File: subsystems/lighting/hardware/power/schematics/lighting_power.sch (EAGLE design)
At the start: 11 parts, among them J1 MOLEX-MICROLOCK-6PIN, J2 MOLEX-MICROLOCK-6PIN, J3 MOLEX-MICROLOCK-6PIN, J4 DCBARRELJACK

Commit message: Lighting V0.3
Fixed daisy-chaining "mirroring" problem
Made DC jack footprint holes smaller (3.3mm->3.1mm dia.)
Made Molex support pads NC
Minor routing updates
Updated silkscreen text
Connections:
- net GND: no longer J1.7, J1.8, J2.7, J2.8, J3.7, J3.8
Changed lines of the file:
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@@
 <part name="TP1" library="Test Point" library_urn="urn:adsk.wipprod:fs.file:vf.-YUoFGRWTEqdap1enj_r5g" deviceset="TP_CIRCLE_2.5MM" device="" package3d_urn="urn:adsk.wipprod:fs.file:vf.3FkuZaG9RiGo42nBWSli3w?version=2" value="GND"/>
 <part name="TP2" library="Test Point" library_urn="urn:adsk.wipprod:fs.file:vf.-YUoFGRWTEqdap1enj_r5g" deviceset="TP_CIRCLE_2.5MM" device="" package3d_urn="urn:adsk.wipprod:fs.file:vf.3FkuZaG9RiGo42nBWSli3w?version=2" value="VCC"/>
+<part name="J4" library="DC Barrel Jack (Locking)" library_urn="urn:adsk.wipprod:fs.file:vf.h4XB8JKWQlqKkOKCMBcezA" deviceset="DCBARRELJACK" device="" package3d_urn="urn:adsk.wipprod:fs.file:vf.mIvCFUCFT52mx3mRBPJ7Ng?version=3"/>
 <part name="J1" library="Molex Micro-Lock PLUS 6-Pin 90deg" library_urn="urn:adsk.wipprod:fs.file:vf.aLnYsiJBRyGIcsa2SAseLA" deviceset="MOLEX-MICROLOCK-6PIN" device="" package3d_urn="urn:adsk.wipprod:fs.file:vf.ZhRZvNezSJa09WGYEOUI9w?version=2"/>
 <part name="J2" library="Molex Micro-Lock PLUS 6-Pin 90deg" library_urn="urn:adsk.wipprod:fs.file:vf.aLnYsiJBRyGIcsa2SAseLA" deviceset="MOLEX-MICROLOCK-6PIN" device="" package3d_urn="urn:adsk.wipprod:fs.file:vf.ZhRZvNezSJa09WGYEOUI9w?version=2"/>
 <part name="J3" library="Molex Micro-Lock PLUS 6-Pin 90deg" library_urn="urn:adsk.wipprod:fs.file:vf.aLnYsiJBRyGIcsa2SAseLA" deviceset="MOLEX-MICROLOCK-6PIN" device="" package3d_urn="urn:adsk.wipprod:fs.file:vf.ZhRZvNezSJa09WGYEOUI9w?version=2"/>
-<part name="J4" library="DC Barrel Jack (Locking)" library_urn="urn:adsk.wipprod:fs.file:vf.h4XB8JKWQlqKkOKCMBcezA" deviceset="DCBARRELJACK" device="" package3d_urn="urn:adsk.wipprod:fs.file:vf.mIvCFUCFT52mx3mRBPJ7Ng?version=3"/>
 </parts>
 <sheets>
@@
 <attribute name="VALUE" x="-40.64" y="-43.18" size="1.778" layer="96" align="bottom-center"/>
 </instance>
+<instance part="J4" gate="G$1" x="-53.34" y="-30.48" smashed="yes">
+<attribute name="NAME" x="-57.542109375" y="-25.77483125" size="1.27246875" layer="95"/>
+</instance>
 <instance part="J1" gate="G$1" x="-38.1" y="5.08" smashed="yes" rot="MR0">
 <attribute name="NAME" x="-42.2656" y="10.3886" size="2.0828" layer="95" ratio="6" rot="SMR0"/>
@@
 <instance part="J3" gate="G$1" x="38.1" y="-66.04" smashed="yes">
 <attribute name="NAME" x="42.2656" y="-60.7314" size="2.0828" layer="95" ratio="6" rot="SR0"/>
-</instance>
-<instance part="J4" gate="G$1" x="-53.34" y="-30.48" smashed="yes">
-<attribute name="NAME" x="-57.542109375" y="-25.77483125" size="1.27246875" layer="95"/>
 </instance>
 </instances>
@@
 <wire x1="-38.1" y1="-7.62" x2="-35.56" y2="-7.62" width="0.1524" layer="91"/>
 <label x="-35.56" y="-7.62" size="1.778" layer="95" rot="R270" xref="yes"/>
-<wire x1="-38.1" y1="-12.7" x2="-38.1" y2="-10.16" width="0.1524" layer="91"/>
 <pinref part="J1" gate="G$1" pin="6"/>
-<junction x="-38.1" y="-7.62"/>
-<pinref part="J1" gate="G$1" pin="7"/>
-<wire x1="-38.1" y1="-10.16" x2="-38.1" y2="-7.62" width="0.1524" layer="91"/>
-<junction x="-38.1" y="-10.16"/>
-<pinref part="J1" gate="G$1" pin="8"/>
 </segment>
 <segment>
@@
 </segment>
 <segment>
-<wire x1="38.1" y1="-7.62" x2="38.1" y2="-10.16" width="0.1524" layer="91"/>
 <label x="38.1" y="-12.7" size="1.778" layer="95" rot="R270" xref="yes"/>
+<wire x1="38.1" y1="-7.62" x2="38.1" y2="-12.7" width="0.1524" layer="91"/>
 <pinref part="J2" gate="G$1" pin="6"/>
-<pinref part="J2" gate="G$1" pin="7"/>
-<wire x1="38.1" y1="-10.16" x2="38.1" y2="-12.7" width="0.1524" layer="91"/>
-<junction x="38.1" y="-10.16"/>
-<pinref part="J2" gate="G$1" pin="8"/>
 </segment>
 <segment>
-<wire x1="38.1" y1="-78.74" x2="38.1" y2="-81.28" width="0.1524" layer="91"/>
 <label x="38.1" y="-83.82" size="1.778" layer="95" rot="R270" xref="yes"/>
+<wire x1="38.1" y1="-78.74" x2="38.1" y2="-83.82" width="0.1524" layer="91"/>
 <pinref part="J3" gate="G$1" pin="6"/>
-<pinref part="J3" gate="G$1" pin="7"/>
-<wire x1="38.1" y1="-81.28" x2="38.1" y2="-83.82" width="0.1524" layer="91"/>
-<junction x="38.1" y="-81.28"/>
-<pinref part="J3" gate="G$1" pin="8"/>
 </segment>
 <segment>

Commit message: Lighting V0.4
FINALLY fixed the connector flipping error (hint: pin 1 goes to pin 6 EVERY TIME)
Flipped LED series order (blue on bottom)
More "bus"-like routing on power PCB
Updated version number text on PCBs
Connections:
- net GND: now also J3.1; no longer J3.6
- net N$11: now also J3.6; no longer J3.1
- net N$12: now also J3.5; no longer J3.2
- net N$13: now also J3.4; no longer J3.3
- net N$14: now also J3.3; no longer J3.4
- net N$15: now also J3.2; no longer J3.5
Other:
- moved on the sheet: J3
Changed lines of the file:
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@@
 <attribute name="NAME" x="42.2656" y="10.3886" size="2.0828" layer="95" ratio="6" rot="SR0"/>
 </instance>
-<instance part="J3" gate="G$1" x="38.1" y="-66.04" smashed="yes">
-<attribute name="NAME" x="42.2656" y="-60.7314" size="2.0828" layer="95" ratio="6" rot="SR0"/>
+<instance part="J3" gate="G$1" x="38.1" y="-78.74" smashed="yes" rot="MR180">
+<attribute name="NAME" x="42.2656" y="-84.0486" size="2.0828" layer="95" ratio="6" rot="SMR180"/>
 </instance>
 </instances>
@@
 <label x="38.1" y="-83.82" size="1.778" layer="95" rot="R270" xref="yes"/>
 <wire x1="38.1" y1="-78.74" x2="38.1" y2="-83.82" width="0.1524" layer="91"/>
-<pinref part="J3" gate="G$1" pin="6"/>
+<pinref part="J3" gate="G$1" pin="1"/>
 </segment>
 <segment>
@@
 <wire x1="17.78" y1="-66.04" x2="38.1" y2="-66.04" width="0.1524" layer="91"/>
 <pinref part="LEDPWR1" gate="G$1" pin="-VOUT"/>
-<pinref part="J3" gate="G$1" pin="1"/>
+<pinref part="J3" gate="G$1" pin="6"/>
 </segment>
 </net>
@@
 <wire x1="20.32" y1="-68.58" x2="38.1" y2="-68.58" width="0.1524" layer="91"/>
 <pinref part="LEDPWR2" gate="G$1" pin="-VOUT"/>
-<pinref part="J3" gate="G$1" pin="2"/>
+<pinref part="J3" gate="G$1" pin="5"/>
 </segment>
 </net>
@@
 <wire x1="22.86" y1="-71.12" x2="38.1" y2="-71.12" width="0.1524" layer="91"/>
 <pinref part="LEDPWR3" gate="G$1" pin="-VOUT"/>
-<pinref part="J3" gate="G$1" pin="3"/>
+<pinref part="J3" gate="G$1" pin="4"/>
 </segment>
 </net>
@@
 <wire x1="15.24" y1="-73.66" x2="38.1" y2="-73.66" width="0.1524" layer="91"/>
 <pinref part="LEDPWR4" gate="G$1" pin="-VOUT"/>
-<pinref part="J3" gate="G$1" pin="4"/>
+<pinref part="J3" gate="G$1" pin="3"/>
 </segment>
 </net>
@@
 <wire x1="35.56" y1="-76.2" x2="38.1" y2="-76.2" width="0.1524" layer="91"/>
 <pinref part="LEDPWR5" gate="G$1" pin="-VOUT"/>
-<pinref part="J3" gate="G$1" pin="5"/>
-</segment>
-</net>
+<pinref part="J3" gate="G$1" pin="2"/>
+</segment>
+</net>

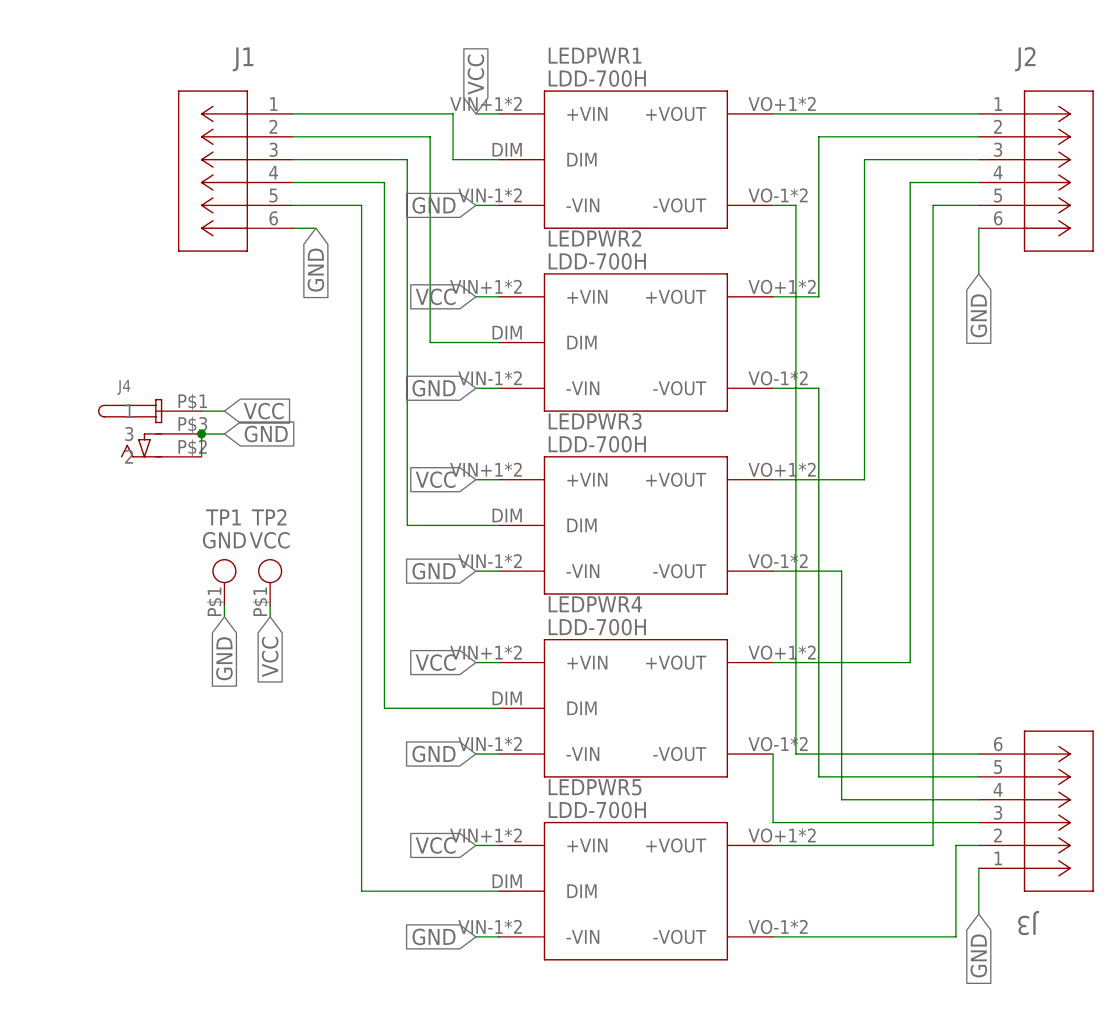
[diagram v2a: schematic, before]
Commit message: Power V0.5 - Module Update
Replaced discontinued module (LDD-H) with SMD package variant (LDD-HS; same functionality)
Board and mount resized, components repositioned
Added PWM pull-down resistors
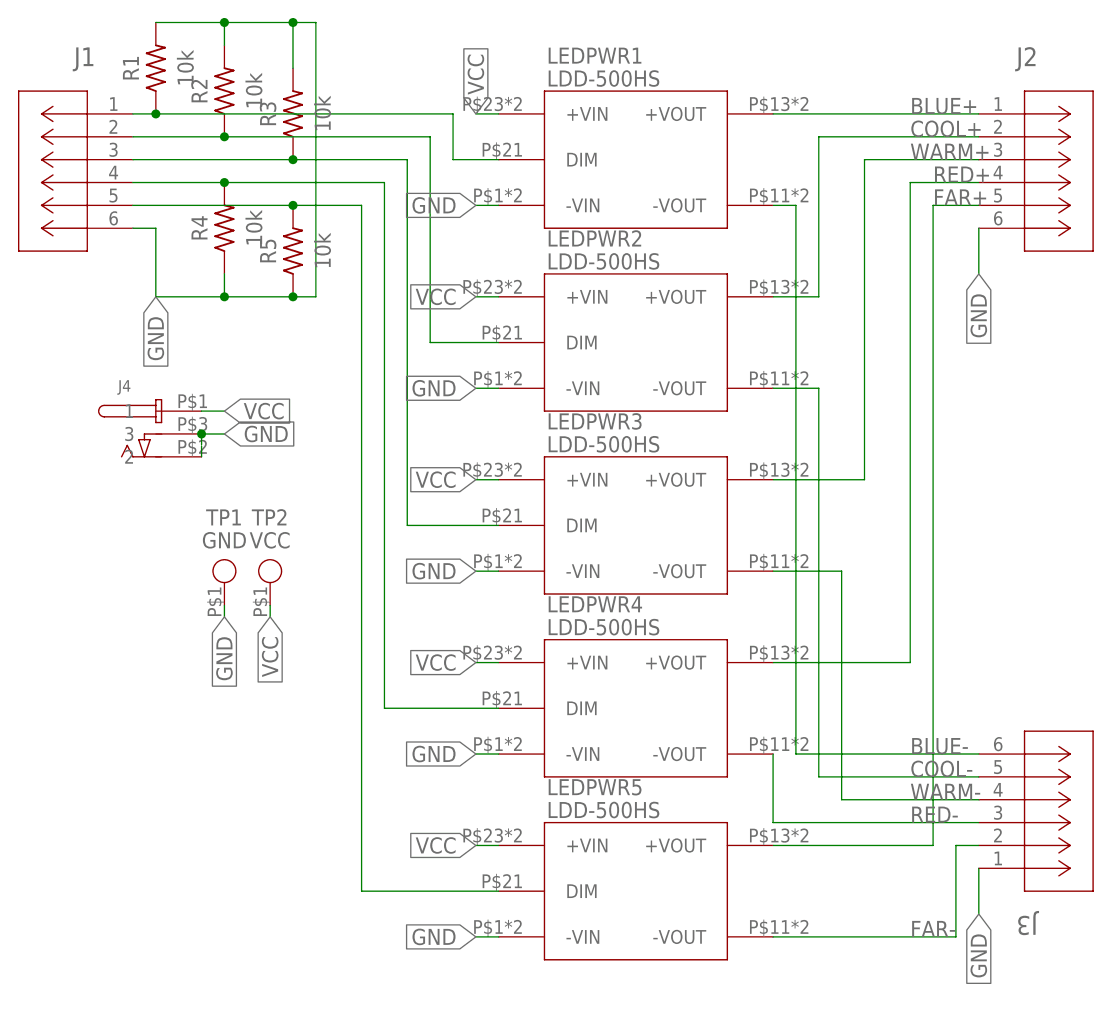
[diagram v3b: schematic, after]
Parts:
- added R1, R2, R3, R4, R5: 10k, Resistor:R-US_CHIP-0402(1005-METRIC)
- LEDPWR1, LEDPWR2, LEDPWR3, LEDPWR4, LEDPWR5: value LDD-700H -> LDD-500HS; device MeanWell NLDD-H Series:NLDD-300~1000H -> MeanWell NLDD-H Series:LDD-300~1000HS
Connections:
- net N$10 renamed FAR+
- net N$11 renamed BLUE-
- net N$12 renamed COOL-
- net N$13 renamed WARM-
- net N$14 renamed RED-
- net N$15 renamed FAR-
- net N$6 renamed BLUE+
- net N$7 renamed COOL+
- net N$8 renamed WARM+
- net N$9 renamed RED+
- net GND: now also R1.2, R2.2, R3.2, R4.1, R5.1
- net N$1: now also R1.1
- net N$2: now also R2.1
- net N$3: now also R3.1
- net N$4: now also R4.2
- net N$5: now also R5.2
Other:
- moved on the sheet: J1, LEDPWR1, LEDPWR2, LEDPWR3, LEDPWR4, LEDPWR5
